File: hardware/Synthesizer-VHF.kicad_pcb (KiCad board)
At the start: 4 copper layers, 50.6 x 50.6 mm, 89 parts, among them J1 Screw_Terminal_01x02, J2 Scope, J4 USB-C 2.0 16P, J5 REF_IN, J6 Scope, J7 RFOUTA, J8 Header 1x3, J9 RFOUTB, U1 LM7805A, U2 FT231XQ, U3 ATtiny1616-M, U4 ADF4351, U5 USBLC6-2SC6, U7 ADP150AUJZ-3.3-R7, U8 ADP150AUJZ-3.3-R7, X1 HCI 8122S-25NQ33FTL

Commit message: diecast-2x2: user layout edits (KiCad save)
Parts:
- moved J5 4.39 mm to (166.9, 76.2)
- moved J9 4.17 mm to (167.0, 113.3)
- moved J7 3.83 mm to (153.6, 113.2)
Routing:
- net Net-(J7-In): track 10.9 -> 12.4 mm
- net Net-(J9-In): track 11.2 -> 12.3 mm
- net GND: vias 206 -> 205
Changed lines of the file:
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@@
 	(footprint "Connector_Coaxial:SMA_Amphenol_901-144_Vertical"
 		(layer "B.Cu")
-		(at 153.84 109.39 180)
+		(at 153.59 113.21 180)
 		(descr "https://www.amphenolrf.com/library/download/link/link_id/593640/parent/901-144/")
 		(tags "SMA THT Female Jack Vertical")
@@
 	(footprint "Connector_Coaxial:SMA_Amphenol_901-144_Vertical"
 		(layer "B.Cu")
-		(at 167.99 80.49 180)
+		(at 166.89 76.24 180)
 		(descr "https://www.amphenolrf.com/library/download/link/link_id/593640/parent/901-144/")
 		(tags "SMA THT Female Jack Vertical")
@@
 	(footprint "Connector_Coaxial:SMA_Amphenol_901-144_Vertical"
 		(layer "B.Cu")
-		(at 167.09 109.14 180)
+		(at 166.99 113.31 180)
 		(descr "https://www.amphenolrf.com/library/download/link/link_id/593640/parent/901-144/")
 		(tags "SMA THT Female Jack Vertical")
@@
 		(layer "Dwgs.User")
 		(pts
-			(xy 130.675 94.85) (xy 177.375 94.85)
-		)
-		(height 0)
-		(format
-			(prefix "")
-			(suffix "")
-			(units 3)
-			(units_format 1)
-			(precision 2)
-		)
-		(style
-			(thickness 0.15)
-			(arrow_length 1.27)
-			(text_position_mode 0)
-			(arrow_direction outward)
-			(extension_height 0.58642)
-			(extension_offset 0.5)
-			(keep_text_aligned yes)
-		)
-		(gr_text "46.70 mm"
-			(at 154.025 93.7 0)
-			(layer "Dwgs.User")
-			(effects
-				(font
-					(size 1 1)
-					(thickness 0.15)
-				)
-			)
-		)
-	)
-	(dimension
-		(type aligned)
-		(layer "Dwgs.User")
-		(pts
-			(xy 134.55 76) (xy 134.55 113.7)
-		)
-		(height 2.65)
-		(format
-			(prefix "")
-			(suffix "")
-			(units 3)
-			(units_format 1)
-			(precision 2)
-		)
-		(style
-			(thickness 0.2)
-			(arrow_length 1.27)
-			(text_position_mode 0)
-			(arrow_direction outward)
-			(extension_height 0.58642)
-			(extension_offset 0.5)
-			(keep_text_aligned yes)
-		)
-		(gr_text "37.70 mm"
-			(at 130.1 94.85 90)
-			(layer "Dwgs.User")
-			(effects
-				(font
-					(size 1.5 1.5)
-					(thickness 0.3)
-				)
-			)
-		)
-	)
-	(dimension
-		(type aligned)
-		(layer "Dwgs.User")
-		(pts
 			(xy 179.3 69.55) (xy 179.3 120.15)
 		)
@@
 	)
 	(via
-		(at 153.7 113.05)
-		(size 0.45)
-		(drill 0.3)
-		(layers "F.Cu" "B.Cu")
-		(free yes)
-		(capping no)
-		(covering
-			(front no)
-			(back no)
-		)
-		(plugging
-			(front no)
-			(back no)
-		)
-		(filling no)
-		(net "GND")
-	)
-	(via
 		(at 178.2375 87.35)
 		(size 0.45)
@@
 	)
 	(segment
-		(start 162.8025 107.388582)
-		(end 164.613918 109.2)
-		(width 0.1565)
-		(layer "F.Cu")
-		(net "Net-(J9-In)")
-	)
-	(segment
-		(start 164.613918 109.2)
-		(end 168.6 109.2)
-		(width 0.1565)
-		(layer "F.Cu")
-		(net "Net-(J9-In)")
-	)
-	(segment
-		(start 162.8025 105.3025)
-		(end 162.8025 107.388582)
-		(width 0.1565)
-		(layer "F.Cu")
-		(net "Net-(J9-In)")
-	)
-	(segment
-		(start 161.098426 103.598426)
-		(end 162.8025 105.3025)
+		(start 161.098426 103.479107)
+		(end 166.99 109.370681)
 		(width 0.1565)
 		(layer "F.Cu")
@@
 	)
 	(segment
-		(start 161.098426 103.479107)
-		(end 161.098426 103.598426)
+		(start 166.99 109.370681)
+		(end 166.99 113.31)
 		(width 0.1565)
 		(layer "F.Cu")
@@
 	)
 	(segment
-		(start 159.2 104.258426)
-		(end 159.2 108.1)
+		(start 153.59 109.868426)
+		(end 153.59 113.21)
 		(width 0.1565)
 		(layer "F.Cu")
@@
 	(segment
 		(start 159.998426 103.46)
-		(end 159.2 104.258426)
-		(width 0.1565)
-		(layer "F.Cu")
-		(net "Net-(J7-In)")
-	)
-	(segment
-		(start 157.91 109.39)
-		(end 153.84 109.39)
-		(width 0.1565)
-		(layer "F.Cu")
-		(net "Net-(J7-In)")
-	)
-	(segment
-		(start 159.2 108.1)
-		(end 157.91 109.39)
+		(end 153.59 109.868426)
 		(width 0.1565)
 		(layer "F.Cu")

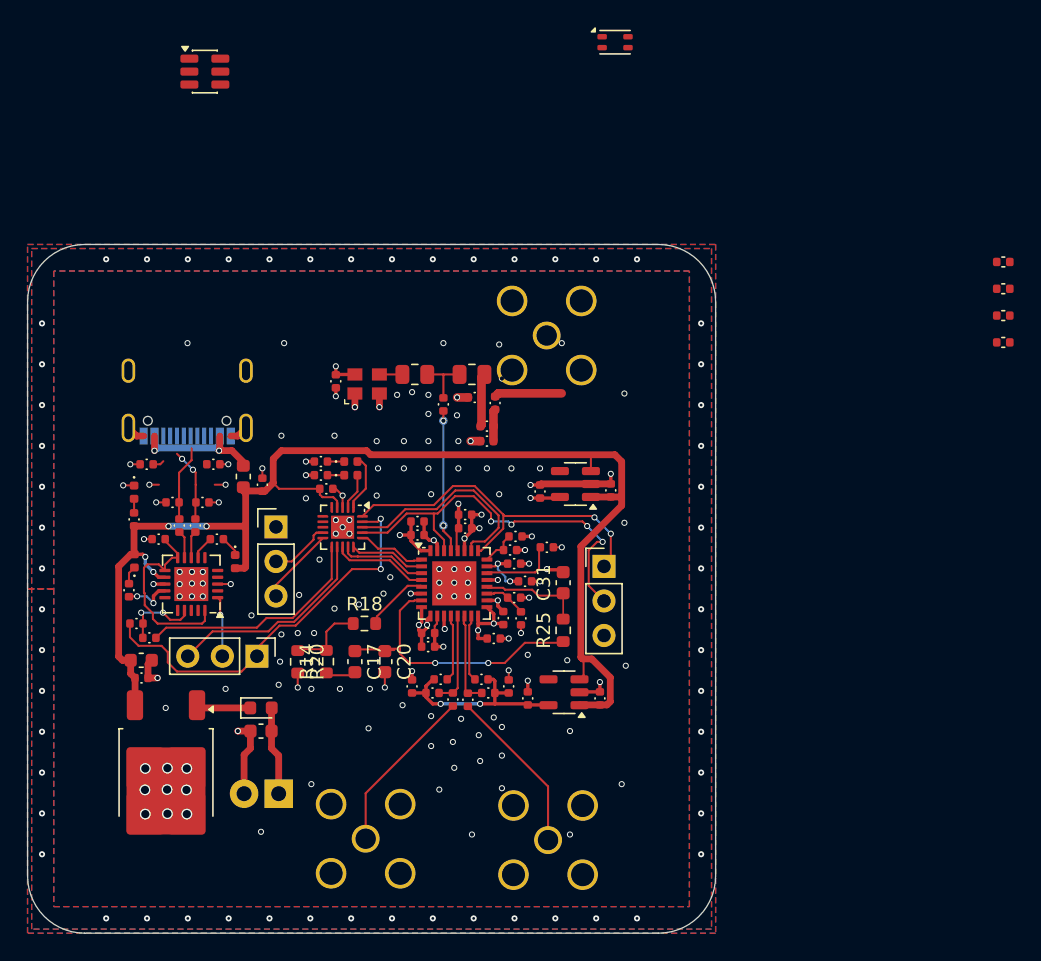
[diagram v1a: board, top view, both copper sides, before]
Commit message: diecast-2x2: restore mounting holes H1-H4 (MountingHole_3.9mm_Pad_D5.6, GND) on 40.5mm square; dropped by Update PCB (no schematic symbols)
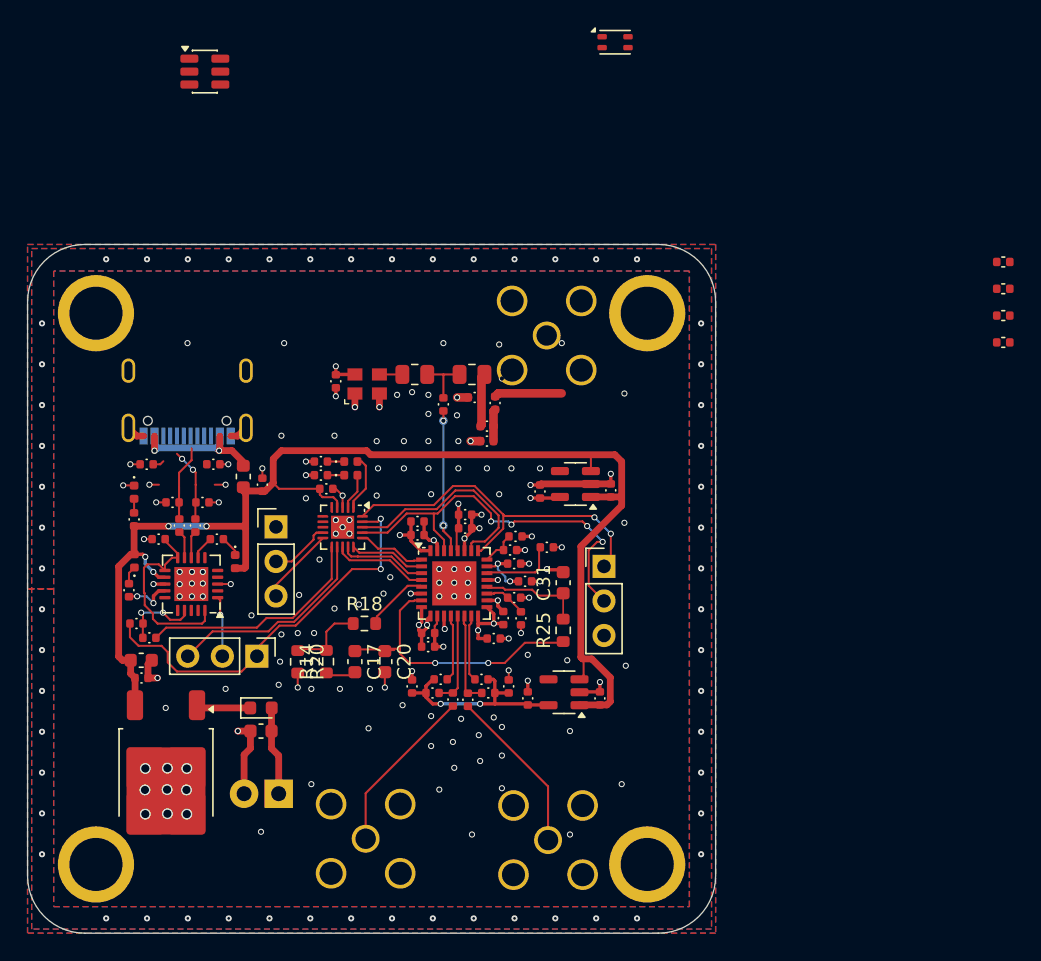
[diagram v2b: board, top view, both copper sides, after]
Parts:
- added H1: MountingHole_6-32, Synthesizer:MountingHole_3.9mm_Pad_D5.6, F.Cu at (133.8, 74.6)
- added H2: MountingHole_6-32, Synthesizer:MountingHole_3.9mm_Pad_D5.6, F.Cu at (174.3, 74.6)
- added H3: MountingHole_6-32, Synthesizer:MountingHole_3.9mm_Pad_D5.6, F.Cu at (174.3, 115.1)
- added H4: MountingHole_6-32, Synthesizer:MountingHole_3.9mm_Pad_D5.6, F.Cu at (133.8, 115.1)

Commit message: diecast-2x2: user layout edits (KiCad save)
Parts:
- moved J4 5.14 mm to (144.1, 76.2)
- moved J5 0.17 mm to (167.1, 76.2)
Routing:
- net GND: track 61.2 -> 58.4 mm, vias 205 -> 204
- net Net-(J5-In): track 4.98 -> 7.18 mm
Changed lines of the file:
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@@
 	(footprint "Synthesizer:MountingHole_3.9mm_Pad_D5.6"
 		(layer "F.Cu")
-		(sheetname "/")
-		(sheetfile "Synthesizer-VHF.kicad_sch")
 		(at 174.275 74.6)
 		(descr "Plated mounting hole, 3.9 mm (Hammond 1590LB lid hole, #6-32 screw), 5.6 mm pad")
@@
 			)
 		)
-		(attr exclude_from_pos_files exclude_from_bom)
+		(property ki_fp_filters "MountingHole*Pad*")
+		(sheetname "/")
+		(sheetfile "Synthesizer-VHF.kicad_sch")
+		(units
+			(unit
+				(name "A")
+				(pins "1")
+			)
+		)
+		(attr exclude_from_bom)
 		(duplicate_pad_numbers_are_jumpers no)
 		(fp_circle
@@
 			(remove_unused_layers no)
 			(net "GND")
+			(pinfunction "1_1")
+			(pintype "input")
 		)
 		(embedded_fonts no)
@@
 	(footprint "Synthesizer:MountingHole_3.9mm_Pad_D5.6"
 		(layer "F.Cu")
-		(sheetname "/")
-		(sheetfile "Synthesizer-VHF.kicad_sch")
 		(at 133.775 115.1)
 		(descr "Plated mounting hole, 3.9 mm (Hammond 1590LB lid hole, #6-32 screw), 5.6 mm pad")
@@
 			)
 		)
-		(attr exclude_from_pos_files exclude_from_bom)
+		(property ki_fp_filters "MountingHole*Pad*")
+		(sheetname "/")
+		(sheetfile "Synthesizer-VHF.kicad_sch")
+		(units
+			(unit
+				(name "A")
+				(pins "1")
+			)
+		)
+		(attr exclude_from_bom)
 		(duplicate_pad_numbers_are_jumpers no)
 		(fp_circle
@@
 			(remove_unused_layers no)
 			(net "GND")
+			(pinfunction "1_1")
+			(pintype "input")
 		)
 		(embedded_fonts no)
@@
 	(footprint "Synthesizer:MountingHole_3.9mm_Pad_D5.6"
 		(layer "F.Cu")
-		(sheetname "/")
-		(sheetfile "Synthesizer-VHF.kicad_sch")
 		(at 174.275 115.1)
 		(descr "Plated mounting hole, 3.9 mm (Hammond 1590LB lid hole, #6-32 screw), 5.6 mm pad")
@@
 			)
 		)
-		(attr exclude_from_pos_files exclude_from_bom)
+		(property ki_fp_filters "MountingHole*Pad*")
+		(sheetname "/")
+		(sheetfile "Synthesizer-VHF.kicad_sch")
+		(units
+			(unit
+				(name "A")
+				(pins "1")
+			)
+		)
+		(attr exclude_from_bom)
 		(duplicate_pad_numbers_are_jumpers no)
 		(fp_circle
@@
 			(remove_unused_layers no)
 			(net "GND")
+			(pinfunction "1_1")
+			(pintype "input")
 		)
 		(embedded_fonts no)
@@
 	(footprint "Synthesizer:MountingHole_3.9mm_Pad_D5.6"
 		(layer "F.Cu")
-		(sheetname "/")
-		(sheetfile "Synthesizer-VHF.kicad_sch")
 		(at 133.775 74.6)
 		(descr "Plated mounting hole, 3.9 mm (Hammond 1590LB lid hole, #6-32 screw), 5.6 mm pad")
@@
 			)
 		)
-		(attr exclude_from_pos_files exclude_from_bom)
+		(property ki_fp_filters "MountingHole*Pad*")
+		(sheetname "/")
+		(sheetfile "Synthesizer-VHF.kicad_sch")
+		(units
+			(unit
+				(name "A")
+				(pins "1")
+			)
+		)
+		(attr exclude_from_bom)
 		(duplicate_pad_numbers_are_jumpers no)
 		(fp_circle
@@
 			(remove_unused_layers no)
 			(net "GND")
+			(pinfunction "1_1")
+			(pintype "input")
 		)
 		(embedded_fonts no)
@@
 	(footprint "Connector_Coaxial:SMA_Amphenol_901-144_Vertical"
 		(layer "B.Cu")
-		(at 166.89 76.24 180)
+		(at 167.06 76.24 180)
 		(descr "https://www.amphenolrf.com/library/download/link/link_id/593640/parent/901-144/")
 		(tags "SMA THT Female Jack Vertical")
@@
 	(footprint "Synthesizer:USB_C_Receptacle_G-Switch_GT-USB-7010ASV"
 		(layer "B.Cu")
-		(at 140.477 79.9)
+		(at 144.07 76.225)
 		(descr "USB Type C, right-angle, SMT, https://datasheet.lcsc.com/lcsc/2204071530_G-Switch-GT-USB-7010ASV_C2988369.pdf")
 		(tags "USB C Type-C Receptacle SMD")
@@
 	)
 	(segment
-		(start 144.197 83.625)
-		(end 144.797 83.025)
-		(width 0.5)
-		(layer "F.Cu")
-		(net "GND")
-	)
-	(segment
 		(start 165.598426 95.498426)
 		(end 164.980893 95.498426)
@@
 	)
 	(segment
-		(start 143.677 83.625)
-		(end 144.197 83.625)
-		(width 0.5)
-		(layer "F.Cu")
-		(net "GND")
-	)
-	(segment
 		(start 142.716074 94.5)
 		(end 143.678574 94.5)
@@
 	)
 	(segment
-		(start 137.277 83.625)
-		(end 137.277 83.7195)
-		(width 0.15)
-		(layer "F.Cu")
-		(net "GND")
-	)
-	(segment
 		(start 165 97.5)
 		(end 165 98.1)
@@
 	)
 	(segment
-		(start 136.757 83.625)
-		(end 136.157 83.025)
-		(width 0.5)
-		(layer "F.Cu")
-		(net "GND")
-	)
-	(segment
 		(start 151.89667 87.998426)
 		(end 151.895898 87.999198)
@@
 	)
 	(segment
-		(start 137.277 83.625)
-		(end 136.757 83.625)
-		(width 0.5)
-		(layer "F.Cu")
-		(net "GND")
-	)
-	(segment
 		(start 158.600456 91.275)
 		(end 158.593 91.282456)
@@
 	)
 	(via
-		(at 163.6 79.4)
-		(size 0.45)
-		(drill 0.3)
-		(layers "F.Cu" "B.Cu")
-		(capping no)
-		(covering
-			(front no)
-			(back no)
-		)
-		(plugging
-			(front no)
-			(back no)
-		)
-		(filling no)
-		(net "GND")
-	)
-	(via
 		(at 147.4 83.6)
 		(size 0.45)
@@
 	)
 	(segment
-		(start 167.99 80.49)
-		(end 163.332467 80.49)
+		(start 167.06 78.562846)
+		(end 164.901953 80.720893)
+		(width 0.635)
+		(layer "F.Cu")
+		(net "Net-(J5-In)")
+	)
+	(segment
+		(start 167.06 76.24)
+		(end 167.06 78.562846)
 		(width 0.635)
 		(layer "F.Cu")
@@
 	)
 	(segment
-		(start 163.332467 80.49)
+		(start 164.901953 80.720893)
 		(end 163.101574 80.720893)
 		(width 0.635)
